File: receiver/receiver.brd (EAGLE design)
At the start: 49.2 x 26.7 mm, 10 parts, among them P1 PROMICRO_HEADER, P2 PROMICRO_HEADER, U1 CORE51822B, U2 AZ1117IH

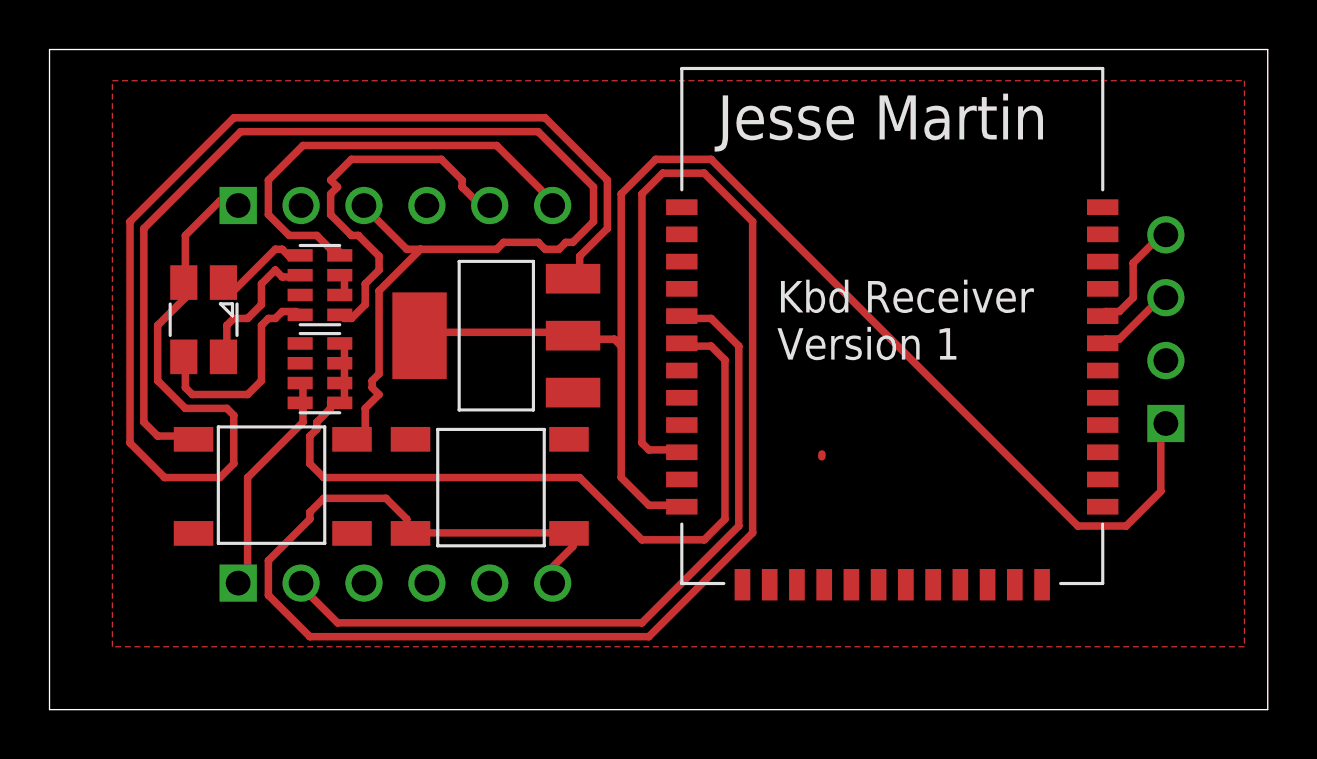
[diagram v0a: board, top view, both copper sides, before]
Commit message: add 2nd layer ground and vias
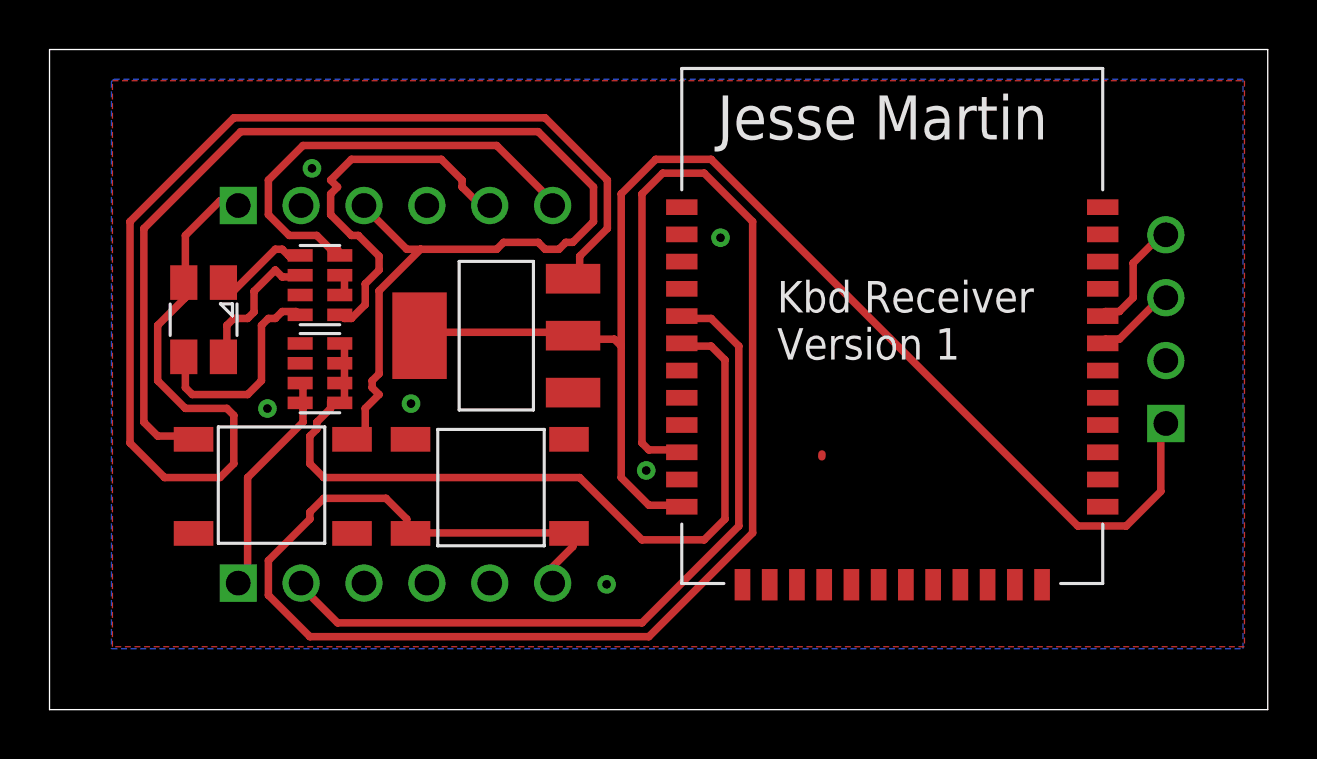
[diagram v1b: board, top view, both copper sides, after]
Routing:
- net GND: vias 0 -> 6
- added copper zone on layer 16, net GND
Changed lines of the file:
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@@
 <setting verticaltext="up"/>
 </settings>
-<grid distance="2.54" unitdist="mm" unit="mm" style="lines" multiple="1" display="yes" altdistance="5" altunitdist="mil" altunit="mil"/>
+<grid distance="0.1" unitdist="mm" unit="mm" style="lines" multiple="1" display="yes" altdistance="5" altunitdist="mil" altunit="mil"/>
 <layers>
 <layer number="1" name="Top" color="4" fill="1" visible="yes" active="yes"/>
-<layer number="16" name="Bottom" color="1" fill="1" visible="no" active="yes"/>
+<layer number="16" name="Bottom" color="1" fill="1" visible="yes" active="yes"/>
 <layer number="17" name="Pads" color="2" fill="1" visible="yes" active="yes"/>
 <layer number="18" name="Vias" color="2" fill="1" visible="yes" active="yes"/>
@@
 <vertex x="40.64" y="43.18"/>
 </polygon>
-<wire x1="63.636" y1="49.934" x2="69.2912" y2="50.8508" width="0" layer="19" extent="1-1"/>
-<wire x1="50.317" y1="47.757" x2="52.68" y2="51.557" width="0" layer="19" extent="1-1"/>
-<wire x1="48.222" y1="55.429" x2="52.68" y2="51.557" width="0" layer="19" extent="1-1"/>
-<wire x1="48.26" y1="61" x2="48.222" y2="55.429" width="0" layer="19" extent="1-1"/>
-<wire x1="63.636" y1="60.934" x2="59.244" y2="53.443" width="0" layer="19" extent="1-1"/>
+<via x="48.7" y="62.5" extent="1-16" drill="0.35"/>
+<via x="65.2" y="59.7" extent="1-16" drill="0.35"/>
+<via x="62.2" y="50.3" extent="1-16" drill="0.35"/>
+<via x="60.6" y="45.7" extent="1-16" drill="0.35"/>
+<via x="52.7" y="53" extent="1-16" drill="0.35"/>
+<via x="46.9" y="52.8" extent="1-16" drill="0.35"/>
+<polygon width="0.1524" layer="16">
+<vertex x="40.6" y="66"/>
+<vertex x="40.6" y="43.1"/>
+<vertex x="86.3" y="43.1"/>
+<vertex x="86.3" y="66.1"/>
+<vertex x="40.7" y="66.1"/>
+</polygon>
 </signal>
 <signal name="VCC">
@@
 <wire x1="47.498" y1="58.1152" x2="48.0568" y2="58.1152" width="0.3048" layer="1"/>
 <wire x1="47.2186" y1="58.3946" x2="47.498" y2="58.1152" width="0.3048" layer="1"/>
-<wire x1="46.6598" y1="57.8358" x2="47.2186" y2="58.3946" width="0.3048" layer="1"/>
-<wire x1="46.6598" y1="56.9976" x2="46.6598" y2="57.8358" width="0.3048" layer="1"/>
-<wire x1="46.101" y1="56.4388" x2="46.6598" y2="56.9976" width="0.3048" layer="1"/>
+<wire x1="46.3598" y1="57.5358" x2="47.2186" y2="58.3946" width="0.3048" layer="1"/>
+<wire x1="46.3598" y1="56.6976" x2="46.3598" y2="57.5358" width="0.3048" layer="1"/>
+<wire x1="46.101" y1="56.4388" x2="46.3598" y2="56.6976" width="0.3048" layer="1"/>
 <wire x1="45.5422" y1="56.4388" x2="46.101" y2="56.4388" width="0.3048" layer="1"/>
 <wire x1="45.2628" y1="56.1594" x2="45.5422" y2="56.4388" width="0.3048" layer="1"/>

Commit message: finish routing vias
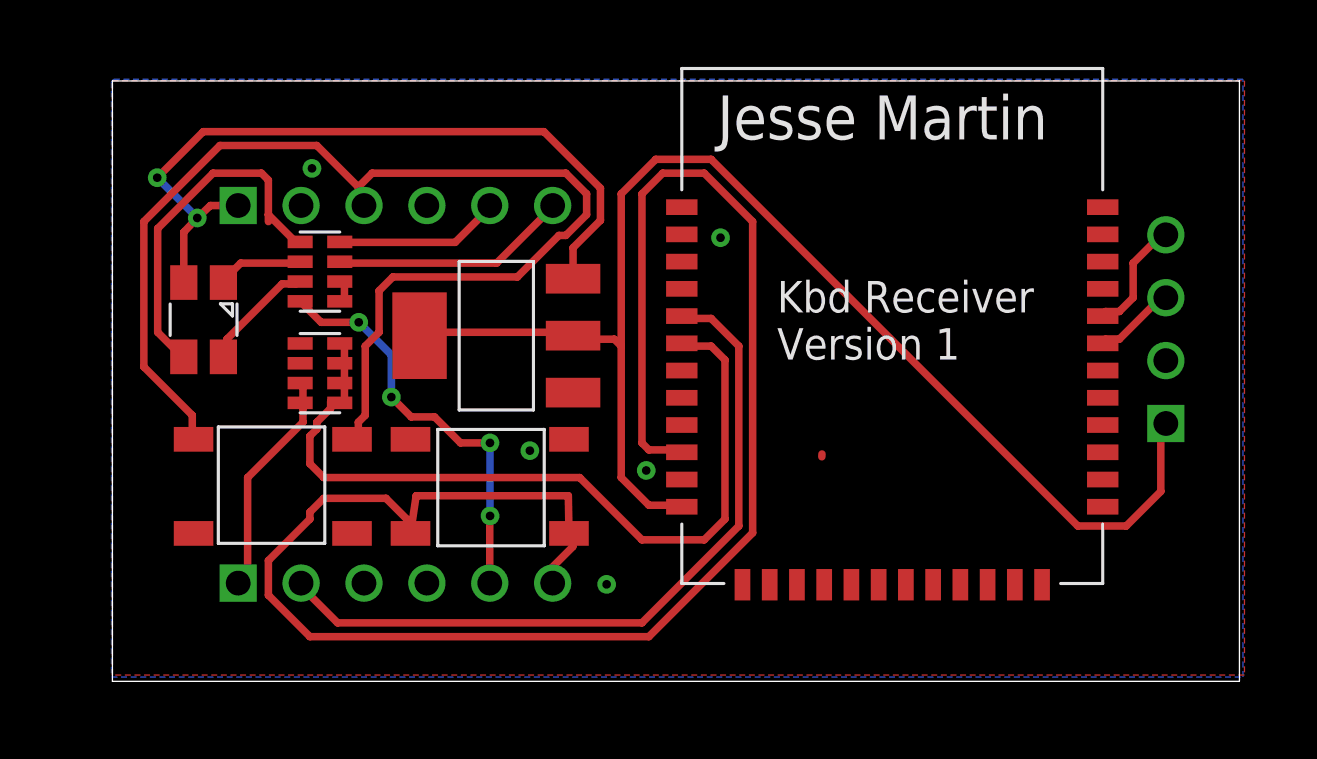
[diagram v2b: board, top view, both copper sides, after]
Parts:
- moved RA1 0.54 mm to (49.0, 58.3)
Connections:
- removed net N$12: RA1.P$2, RA1.P$3
- new net N$2: RA1.P$3, RA1.P$4
- net LED-B: now also RA1.P$1; no longer RA1.P$4
- net LED-G: now also RA1.P$8; no longer RA1.P$7
- net LED-R: now also RA1.P$2; no longer RA1.P$1
- net N$10: now also RA1.P$7; no longer RA1.P$6
- net N$11: now also RA1.P$6; no longer RA1.P$5
- net N$14: now also RA1.P$5; no longer RA1.P$8
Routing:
- net VIN: track 55.4 -> 30.8 mm, vias 0 -> 2
- net LED-G: track 0.00 -> 16.7 mm, vias 0 -> 4
- net LED-B: track 15.6 -> 6.73 mm
- net LED-R: track 18.2 -> 9.60 mm
- net N$14: track 8.75 -> 14.6 mm
- net RESET: track 52.1 -> 47.8 mm
- net PAIR: track 70.0 -> 72.8 mm
- net N$10: track 5.83 -> 4.68 mm
- net N$12: track 1.02 -> 0.00 mm
- net N$2: track 0.00 -> 1.01 mm
- net N$11: track 4.32 -> 3.47 mm
- net GND: vias 6 -> 5
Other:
- board size 49.2 x 26.7 mm -> 45.5 x 24.2 mm

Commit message: update drill size to 10mil
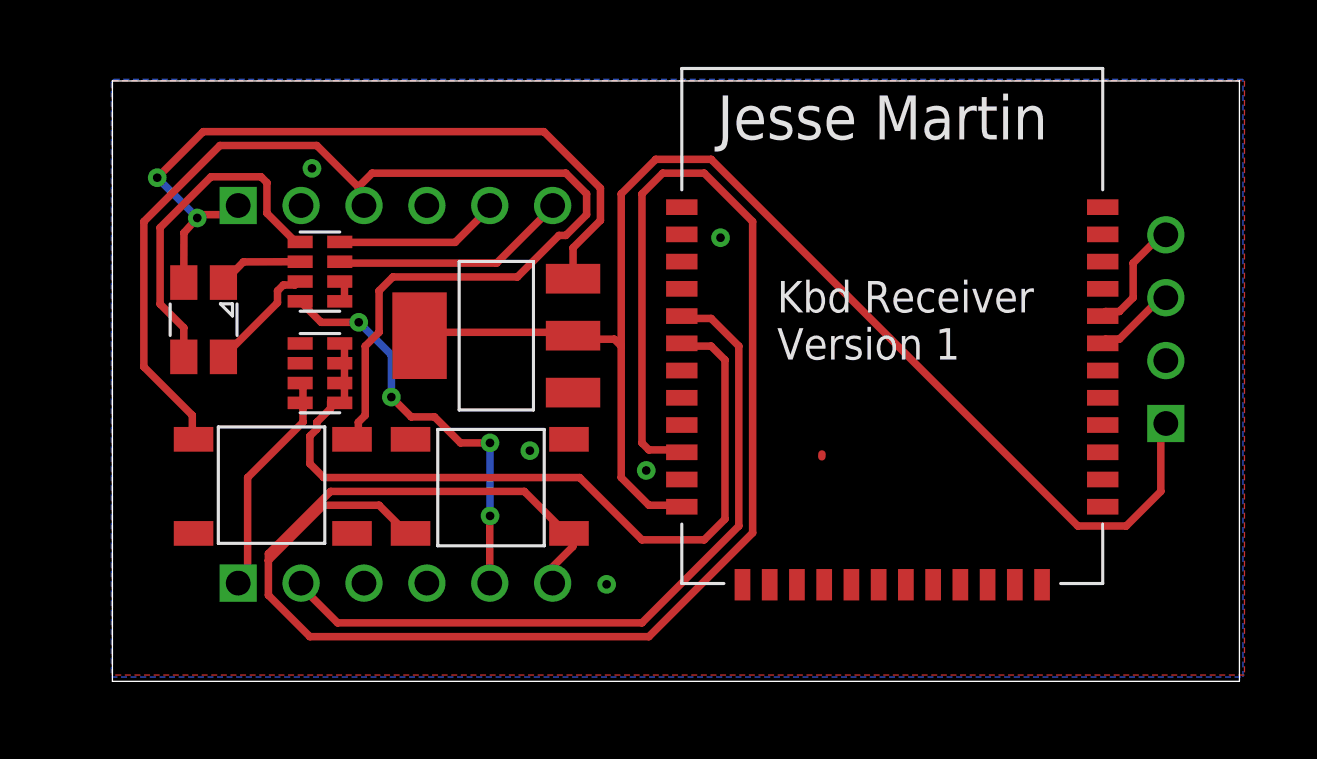
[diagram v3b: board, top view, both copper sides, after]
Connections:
- net N$10: now also D1.GREEN; no longer D1.P$4
- net N$11: now also D1.RED; no longer D1.P$1
- net N$14: now also D1.BLUE; no longer D1.P$3
- net VIN: now also D1.ANODE; no longer D1.P$2
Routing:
- net PAIR: track 72.8 -> 77.1 mm
- net N$14: track 14.6 -> 13.9 mm
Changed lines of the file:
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@@
 <layer number="16" name="Bottom" color="1" fill="1" visible="yes" active="yes"/>
 <layer number="17" name="Pads" color="2" fill="1" visible="yes" active="yes"/>
-<layer number="18" name="Vias" color="2" fill="1" visible="no" active="yes"/>
+<layer number="18" name="Vias" color="2" fill="1" visible="yes" active="yes"/>
 <layer number="19" name="Unrouted" color="6" fill="1" visible="yes" active="yes"/>
 <layer number="20" name="Dimension" color="24" fill="1" visible="yes" active="yes"/>
@@
 </variantdefs>
 <classes>
-<class number="0" name="default" width="0.3048" drill="0.508">
+<class number="0" name="default" width="0.3048" drill="0.254">
 <clearance class="0" value="0.254"/>
 </class>
@@
 </signal>
 <signal name="N$11">
-<contactref element="D1" pad="P$1"/>
+<contactref element="D1" pad="RED"/>
 <contactref element="RA1" pad="P$6"/>
-<wire x1="45.8216" y1="58.674" x2="48.0568" y2="58.674" width="0.3048" layer="1"/>
-<wire x1="45.2628" y1="58.1152" x2="45.8216" y2="58.674" width="0.3048" layer="1"/>
-<wire x1="48.0568" y1="58.674" x2="48.222" y2="58.729659375" width="0.3048" layer="1"/>
-<wire x1="45.2628" y1="58.1152" x2="45.123" y2="57.888" width="0.3048" layer="1"/>
+<wire x1="48.222" y1="58.729659375" x2="48.0568" y2="58.674" width="0.3048" layer="1"/>
+<wire x1="45.123" y1="57.888" x2="45.931265625" y2="58.72306875" width="0.3048" layer="1"/>
+<wire x1="45.931265625" y1="58.72306875" x2="48.222" y2="58.729659375" width="0.3048" layer="1"/>
 </signal>
 <signal name="N$10">
-<contactref element="D1" pad="P$4"/>
+<contactref element="D1" pad="GREEN"/>
 <contactref element="RA1" pad="P$7"/>
-<wire x1="47.498" y1="57.8358" x2="48.0568" y2="57.8358" width="0.3048" layer="1"/>
-<wire x1="45.2628" y1="55.6006" x2="47.498" y2="57.8358" width="0.3048" layer="1"/>
-<wire x1="45.2628" y1="55.0418" x2="45.2628" y2="55.6006" width="0.3048" layer="1"/>
 <wire x1="48.0568" y1="57.8358" x2="48.222" y2="57.929659375" width="0.3048" layer="1"/>
-<wire x1="45.2628" y1="55.0418" x2="45.123" y2="54.888" width="0.3048" layer="1"/>
+<wire x1="47.3076" y1="57.0726" x2="47.3076" y2="57.55199375" width="0.3048" layer="1"/>
+<wire x1="47.3076" y1="57.55199375" x2="47.5456625" y2="57.79005625" width="0.3048" layer="1"/>
+<wire x1="47.5456625" y1="57.79005625" x2="48.01105625" y2="57.79005625" width="0.3048" layer="1"/>
+<wire x1="48.01105625" y1="57.79005625" x2="48.0568" y2="57.8358" width="0.3048" layer="1"/>
+<wire x1="45.123" y1="54.888" x2="47.3076" y2="57.0726" width="0.3048" layer="1"/>
 </signal>
 <signal name="N$14">
-<contactref element="D1" pad="P$3"/>
+<contactref element="D1" pad="BLUE"/>
 <contactref element="RA1" pad="P$5"/>
-<wire x1="46.9392" y1="62.0268" x2="46.9392" y2="60.6298" width="0.3048" layer="1"/>
-<wire x1="46.9392" y1="60.6298" x2="46.9392" y2="60.3504" width="0.3048" layer="1"/>
-<wire x1="46.6598" y1="62.3062" x2="46.9392" y2="62.0268" width="0.3048" layer="1"/>
-<wire x1="44.704" y1="62.3062" x2="46.6598" y2="62.3062" width="0.3048" layer="1"/>
-<wire x1="42.4688" y1="60.071" x2="44.704" y2="62.3062" width="0.3048" layer="1"/>
-<wire x1="42.4688" y1="55.88" x2="42.4688" y2="60.071" width="0.3048" layer="1"/>
-<wire x1="43.307" y1="55.0418" x2="42.4688" y2="55.88" width="0.3048" layer="1"/>
-<wire x1="43.307" y1="55.0418" x2="43.523" y2="54.888" width="0.3048" layer="1"/>
-<wire x1="46.9392" y1="60.6298" x2="48.0568" y2="59.5122" width="0.3048" layer="1"/>
 <wire x1="48.0568" y1="59.5122" x2="48.222" y2="59.529659375" width="0.3048" layer="1"/>
+<wire x1="46.6423375" y1="62.1604" x2="46.8804" y2="61.9223375" width="0.3048" layer="1"/>
+<wire x1="42.5666" y1="57.0196625" x2="42.5666" y2="60.10571875" width="0.3048" layer="1"/>
+<wire x1="42.5666" y1="60.10571875" x2="44.62128125" y2="62.1604" width="0.3048" layer="1"/>
+<wire x1="44.62128125" y1="62.1604" x2="46.6423375" y2="62.1604" width="0.3048" layer="1"/>
+<wire x1="46.8804" y1="61.9223375" x2="46.8804" y2="60.6886" width="0.3048" layer="1"/>
+<wire x1="46.8804" y1="60.6886" x2="48.0568" y2="59.5122" width="0.3048" layer="1"/>
+<wire x1="43.523" y1="56.0632625" x2="42.5666" y2="57.0196625" width="0.3048" layer="1"/>
+<wire x1="43.523" y1="54.888" x2="43.523" y2="56.0632625" width="0.3048" layer="1"/>
 </signal>
 <signal name="RESET">
@@
 <wire x1="46.9392" y1="45.2628" x2="48.6156" y2="43.5864" width="0.3048" layer="1"/>
 <wire x1="46.9392" y1="46.6598" x2="46.9392" y2="45.2628" width="0.3048" layer="1"/>
-<wire x1="48.6156" y1="48.3362" x2="46.9392" y2="46.6598" width="0.3048" layer="1"/>
-<wire x1="48.6156" y1="48.6156" x2="48.6156" y2="48.3362" width="0.3048" layer="1"/>
-<wire x1="49.1744" y1="49.1744" x2="48.6156" y2="48.6156" width="0.3048" layer="1"/>
-<wire x1="51.689" y1="49.1744" x2="49.1744" y2="49.1744" width="0.3048" layer="1"/>
-<wire x1="52.5272" y1="48.3362" x2="51.689" y2="49.1744" width="0.3048" layer="1"/>
-<wire x1="52.5272" y1="47.7774" x2="52.5272" y2="48.3362" width="0.3048" layer="1"/>
 <wire x1="63.4238" y1="51.1302" x2="63.636" y2="51.034" width="0.3048" layer="1"/>
+<wire x1="51.4096" y1="48.895" x2="52.5272" y2="47.7774" width="0.3048" layer="1"/>
+<wire x1="49.1744" y1="48.895" x2="51.4096" y2="48.895" width="0.3048" layer="1"/>
+<wire x1="46.9392" y1="46.6598" x2="49.1744" y2="48.895" width="0.3048" layer="1"/>
 <wire x1="52.5272" y1="47.7774" x2="52.68" y2="47.757" width="0.3048" layer="1"/>
-<wire x1="52.9066" y1="49.2774" x2="59.0534" y2="49.2774" width="0.3048" layer="1"/>
-<wire x1="59.0534" y1="49.2774" x2="59.08" y2="47.757" width="0.3048" layer="1"/>
-<wire x1="52.9066" y1="49.2774" x2="52.68" y2="47.757" width="0.3048" layer="1"/>
+<wire x1="46.9392" y1="46.9392" x2="46.9392" y2="46.6598" width="0.3048" layer="1"/>
+<wire x1="49.4538" y1="49.4538" x2="46.9392" y2="46.9392" width="0.3048" layer="1"/>
+<wire x1="57.277" y1="49.4538" x2="49.4538" y2="49.4538" width="0.3048" layer="1"/>
+<wire x1="58.9534" y1="47.7774" x2="57.277" y2="49.4538" width="0.3048" layer="1"/>
+<wire x1="58.9534" y1="47.7774" x2="59.08" y2="47.757" width="0.3048" layer="1"/>
 </signal>
 <signal name="TXO">
@@
 <signal name="VIN">
 <contactref element="P2" pad="P$1"/>
-<contactref element="D1" pad="P$2"/>
+<contactref element="D1" pad="ANODE"/>
 <contactref element="U2" pad="INPUT"/>
 <via x="44.067034375" y="60.49655625" extent="1-16" drill="0.35"/>
@@
 <wire x1="59.244" y1="59.29193125" x2="59.244" y2="58.043" width="0.3048" layer="1"/>
 <wire x1="58.06726875" y1="63.9826" x2="60.3504" y2="61.69946875" width="0.3048" layer="1"/>
-<wire x1="45.72" y1="61" x2="44.6" y2="61" width="0.3048" layer="1"/>
-<wire x1="44.6" y1="61" x2="44.067034375" y2="60.49655625" width="0.3048" layer="1"/>
-<wire x1="44.067034375" y1="60.49655625" x2="43.523" y2="59.923" width="0.3048" layer="1"/>
-<wire x1="43.523" y1="59.923" x2="43.523" y2="57.888" width="0.3048" layer="1"/>
 <wire x1="42.44960625" y1="62.1235875" x2="44.30861875" y2="63.9826" width="0.3048" layer="1"/>
 <wire x1="44.30861875" y1="63.9826" x2="58.06726875" y2="63.9826" width="0.3048" layer="1"/>
 <wire x1="42.44960625" y1="62.1235875" x2="44.067034375" y2="60.506159375" width="0.3048" layer="16"/>
 <wire x1="44.067034375" y1="60.506159375" x2="44.067034375" y2="60.49655625" width="0.3048" layer="16"/>
+<wire x1="45.2628" y1="60.6298" x2="44.1452" y2="60.6298" width="0.3048" layer="1"/>
+<wire x1="45.5422" y1="60.9092" x2="45.2628" y2="60.6298" width="0.3048" layer="1"/>
+<wire x1="44.1452" y1="60.6298" x2="44.067034375" y2="60.49655625" width="0.3048" layer="1"/>
+<wire x1="45.5422" y1="60.9092" x2="45.72" y2="61" width="0.3048" layer="1"/>
+<wire x1="44.067034375" y1="60.49655625" x2="43.52915625" y2="59.897625" width="0.3048" layer="1"/>
+<wire x1="43.52915625" y1="59.897625" x2="43.523" y2="57.888" width="0.3048" layer="1"/>
 </signal>
 <signal name="RXI">
